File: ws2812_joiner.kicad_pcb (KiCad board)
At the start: 2 copper layers, 7.9 x 132.1 mm, 22 parts, among them P1 CONN_01X03, P10 CONN_01X03, P2 CONN_01X03, P3 CONN_01X03, P4 CONN_01X03, P5 CONN_01X03, P6 CONN_01X03, P7 CONN_01X03, P8 CONN_01X03, P9 CONN_01X03

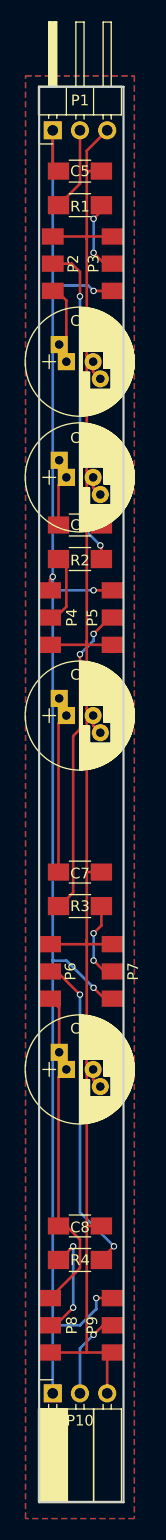
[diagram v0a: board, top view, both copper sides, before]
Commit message: Version 2 - use SMD tantalum caps to neaten everything up. Duplicate silkscreen graphics to the front where possible and add component values.
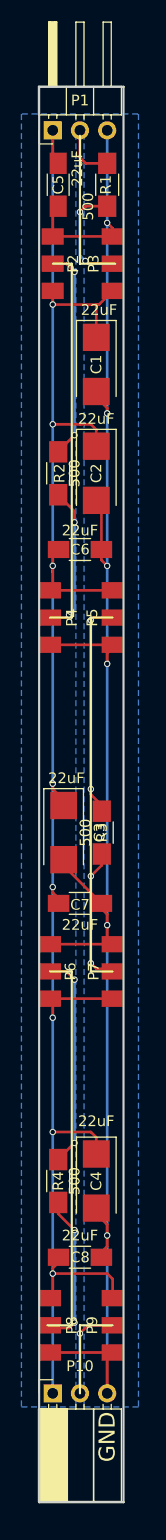
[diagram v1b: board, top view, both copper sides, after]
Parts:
- C1, C2, C3, C4: value CP1 -> 22uF; footprint Capacitors_ThroughHole:CP_Radial_D10.0mm_P2.50mm_P5.00mm -> Capacitors_Tantalum_SMD:CP_Tantalum_Case-C_EIA-6032-28_Reflow
- C5, C6, C7, C8: value CP1 -> 22uF
- R1, R2, R3, R4: value R -> 500
- moved C3 10.9 mm to (150.4, 105.7), turned to 270 degrees
- moved C4 10.8 mm to (153.4, 138.2), turned to 270 degrees
- moved R2 8.26 mm to (149.9, 72.1), turned to 270 degrees
- moved R4 7.64 mm to (149.9, 138.2), turned to 270 degrees
- moved R3 7.15 mm to (153.9, 105.7), turned to 270 degrees
- moved R1 3.17 mm to (154.4, 45.2), turned to 270 degrees
- moved C8 2.92 mm to (151.9, 145.3)
- moved C7 2.92 mm to (151.9, 112.3)
- moved C2 2.82 mm to (153.4, 72.1), turned to 270 degrees
- moved C1 2.81 mm to (153.4, 62.0), turned to 270 degrees
- moved C5 2.40 mm to (149.9, 45.2), turned to 270 degrees
- moved C6 2.29 mm to (151.9, 79.2)
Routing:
- net VCC: track 220.2 -> 179.4 mm, vias 5 -> 8
- net GND: track 158.6 -> 178.1 mm, vias 0 -> 6
- net Net-(P2-Pad2): track 30.5 -> 19.8 mm
- net Net-(P6-Pad2): track 30.3 -> 20.0 mm
- net Net-(P5-Pad2): track 29.2 -> 20.4 mm
- net Net-(P4-Pad2): track 6.69 -> 13.9 mm, vias 0 -> 2
- net Net-(P3-Pad2): track 6.95 -> 12.5 mm
- net Net-(P7-Pad2): track 7.58 -> 13.0 mm
- net Net-(P8-Pad2): track 10.4 -> 14.4 mm
- net Net-(P1-Pad2): track 7.81 -> 5.30 mm
- net Net-(P10-Pad2): track 8.13 -> 8.95 mm
- added copper zone on B.Cu, net GND
- removed copper zone on F.Cu, net GND
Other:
- board text added: "ws2812 Joiner v0.2"
- board text removed: "ws2812 Joiner v0.1"

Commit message: Add GitHub URL to v0.2.
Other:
- board text added: "https://github.com/mooped/LED-Fireplace"
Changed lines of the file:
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@@
     (area 144.821 -534.202481 1425.293211 168.763001)
     (thickness 1.6)
-    (drawings 167)
+    (drawings 168)
     (tracks 174)
     (zones 0)
@@
       (rotate (xyz 0 0 0))
     )
+  )
+  (gr_text https://github.com/mooped/LED-Fireplace (at 154.178 128.27 90) (layer B.SilkS)
+    (effects (font (size 1.5 1.5) (thickness 0.3)) (justify mirror))
   )
   (gr_line (start 151.892 151.638) (end 151.892 157.988) (angle 90) (layer F.SilkS) (width 0.2))
@@
   (gr_line (start 1417.24321 -529.15248) (end 1425.24321 -529.15248) (layer Dwgs.User) (width 0.1))
   (gr_line (start 1417.24321 -529.15248) (end 1417.24321 -430.15248) (layer Dwgs.User) (width 0.1))
-  (gr_text "Steve Barnett 2018" (at 154.686 109.22 90) (layer B.SilkS)
+  (gr_text "Steve Barnett 2018" (at 154.432 60.198 90) (layer B.SilkS)
     (effects (font (size 1.5 1.5) (thickness 0.3)) (justify mirror))
   )
-  (gr_text "ws2812 Joiner v0.2" (at 149.352 109.22 90) (layer B.SilkS)
+  (gr_text "ws2812 Joiner v0.2" (at 149.606 60.198 90) (layer B.SilkS)
     (effects (font (size 1.5 1.5) (thickness 0.3)) (justify mirror))
   )
